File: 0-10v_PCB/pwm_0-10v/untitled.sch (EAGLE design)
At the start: 3 parts, among them U1 OP07CDR

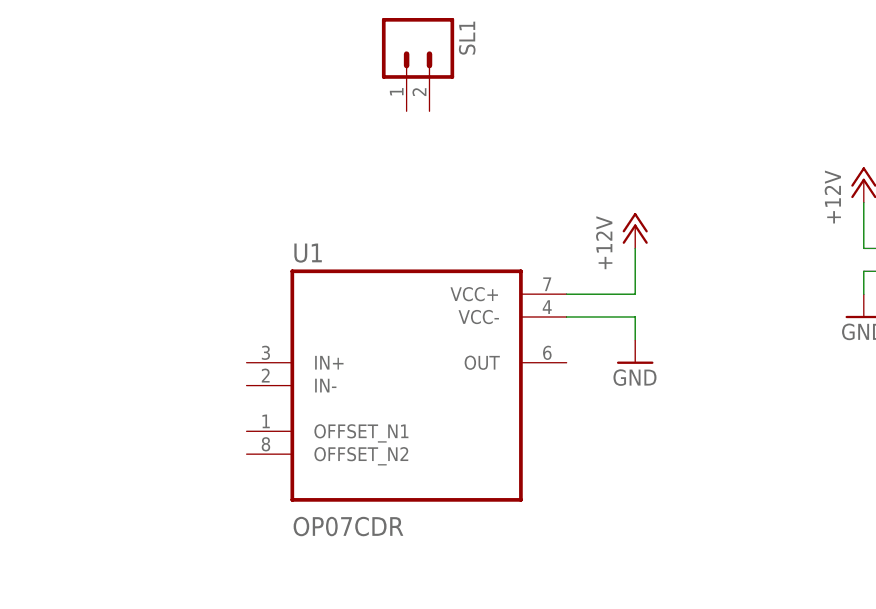
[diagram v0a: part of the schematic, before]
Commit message: added analog circuitry
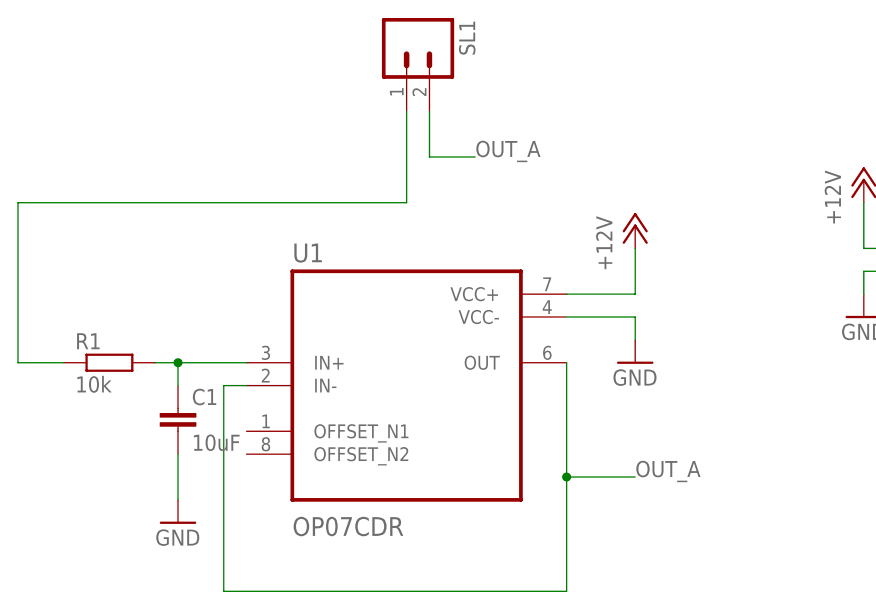
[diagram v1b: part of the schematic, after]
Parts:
- added C1: 10uF, rcl:C-EUC0805
- added R1: 10k, rcl:R-EU_M0805
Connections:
- new net N$1: R1.1, SL1.1
- new net N$2: C1.1, R1.2, U1.IN+
- new net N$3: SL1.2
- new net OUT_A: U1.IN-, U1.OUT
- net GND: now also C1.2
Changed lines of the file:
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@@
 <part name="P+2" library="supply1" library_urn="urn:adsk.eagle:library:371" deviceset="+12V" device=""/>
 <part name="GND2" library="supply1" library_urn="urn:adsk.eagle:library:371" deviceset="GND" device=""/>
+<part name="R1" library="rcl" library_urn="urn:adsk.eagle:library:334" deviceset="R-EU_" device="M0805" package3d_urn="urn:adsk.eagle:package:23556/2" value="10k"/>
+<part name="C1" library="rcl" library_urn="urn:adsk.eagle:library:334" deviceset="C-EU" device="C0805" package3d_urn="urn:adsk.eagle:package:23617/2" value="10uF"/>
+<part name="GND3" library="supply1" library_urn="urn:adsk.eagle:library:371" deviceset="GND" device=""/>
 </parts>
 <sheets>
@@
 <attribute name="VALUE" x="83.82" y="71.12" size="1.778" layer="96"/>
 </instance>
+<instance part="R1" gate="G$1" x="27.94" y="73.66" smashed="yes">
+<attribute name="NAME" x="24.13" y="75.1586" size="1.778" layer="95"/>
+<attribute name="VALUE" x="24.13" y="70.358" size="1.778" layer="96"/>
+</instance>
+<instance part="C1" gate="G$1" x="35.56" y="68.58" smashed="yes">
+<attribute name="NAME" x="37.084" y="68.961" size="1.778" layer="95"/>
+<attribute name="VALUE" x="37.084" y="63.881" size="1.778" layer="96"/>
+</instance>
+<instance part="GND3" gate="1" x="35.56" y="55.88" smashed="yes">
+<attribute name="VALUE" x="33.02" y="53.34" size="1.778" layer="96"/>
+</instance>
 </instances>
 <busses>
@@
 <wire x1="86.36" y1="78.74" x2="86.36" y2="76.2" width="0.1524" layer="91"/>
 </segment>
+<segment>
+<pinref part="C1" gate="G$1" pin="2"/>
+<pinref part="GND3" gate="1" pin="GND"/>
+<wire x1="35.56" y1="63.5" x2="35.56" y2="58.42" width="0.1524" layer="91"/>
+</segment>
 </net>
 <net name="+12V" class="0">
@@
 <pinref part="P+2" gate="1" pin="+12V"/>
 <wire x1="86.36" y1="81.28" x2="86.36" y2="86.36" width="0.1524" layer="91"/>
+</segment>
+</net>
+<net name="N$1" class="0">
+<segment>
+<pinref part="SL1" gate="G$1" pin="1"/>
+<wire x1="60.96" y1="101.6" x2="60.96" y2="91.44" width="0.1524" layer="91"/>
+<wire x1="60.96" y1="91.44" x2="17.78" y2="91.44" width="0.1524" layer="91"/>
+<wire x1="17.78" y1="91.44" x2="17.78" y2="73.66" width="0.1524" layer="91"/>
+<pinref part="R1" gate="G$1" pin="1"/>
+<wire x1="17.78" y1="73.66" x2="22.86" y2="73.66" width="0.1524" layer="91"/>
+</segment>
+</net>
+<net name="N$2" class="0">
+<segment>
+<pinref part="R1" gate="G$1" pin="2"/>
+<pinref part="U1" gate="A" pin="IN+"/>
+<wire x1="33.02" y1="73.66" x2="35.56" y2="73.66" width="0.1524" layer="91"/>
+<pinref part="C1" gate="G$1" pin="1"/>
+<wire x1="35.56" y1="73.66" x2="43.18" y2="73.66" width="0.1524" layer="91"/>
+<wire x1="35.56" y1="71.12" x2="35.56" y2="73.66" width="0.1524" layer="91"/>
+<junction x="35.56" y="73.66"/>
+</segment>
+</net>
+<net name="OUT_A" class="0">
+<segment>
+<pinref part="U1" gate="A" pin="IN-"/>
+<wire x1="43.18" y1="71.12" x2="40.64" y2="71.12" width="0.1524" layer="91"/>
+<wire x1="40.64" y1="71.12" x2="40.64" y2="48.26" width="0.1524" layer="91"/>
+<wire x1="40.64" y1="48.26" x2="78.74" y2="48.26" width="0.1524" layer="91"/>
+<pinref part="U1" gate="A" pin="OUT"/>
+<wire x1="78.74" y1="48.26" x2="78.74" y2="60.96" width="0.1524" layer="91"/>
+<wire x1="78.74" y1="60.96" x2="78.74" y2="73.66" width="0.1524" layer="91"/>
+<wire x1="78.74" y1="60.96" x2="86.36" y2="60.96" width="0.1524" layer="91"/>
+<junction x="78.74" y="60.96"/>
+<label x="86.36" y="60.96" size="1.778" layer="95"/>
+<label x="68.58" y="96.52" size="1.778" layer="95"/>
+</segment>
+</net>
+<net name="N$3" class="0">
+<segment>
+<pinref part="SL1" gate="G$1" pin="2"/>
+<wire x1="63.5" y1="101.6" x2="63.5" y2="96.52" width="0.1524" layer="91"/>
+<wire x1="63.5" y1="96.52" x2="68.58" y2="96.52" width="0.1524" layer="91"/>
 </segment>
 </net>
@@
 packages will not be understood (or retained) with this version.
 </note>
+<note version="8.4" severity="warning">
+Since Version 8.4, EAGLE supports properties for SPICE simulation.
+Probes in schematics and SPICE mapping objects found in parts and library devices
+will not be understood with this version. Update EAGLE to the latest version
+for full support of SPICE simulation.
+</note>
 </compatibility>

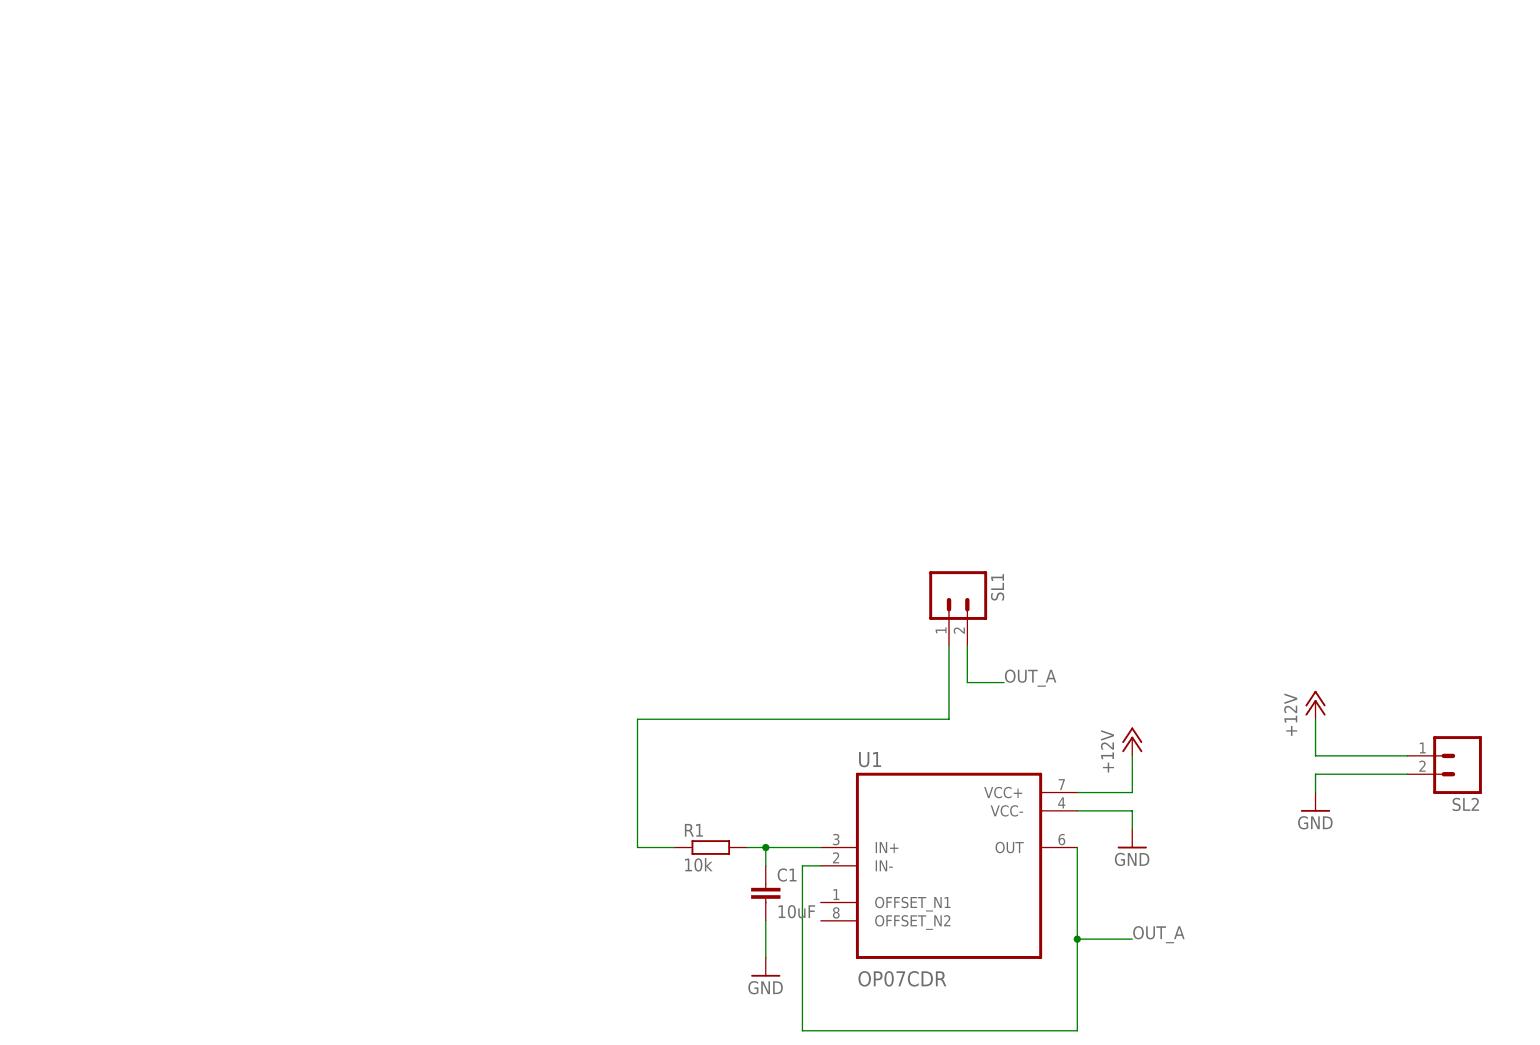
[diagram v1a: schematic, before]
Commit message: part placement completed
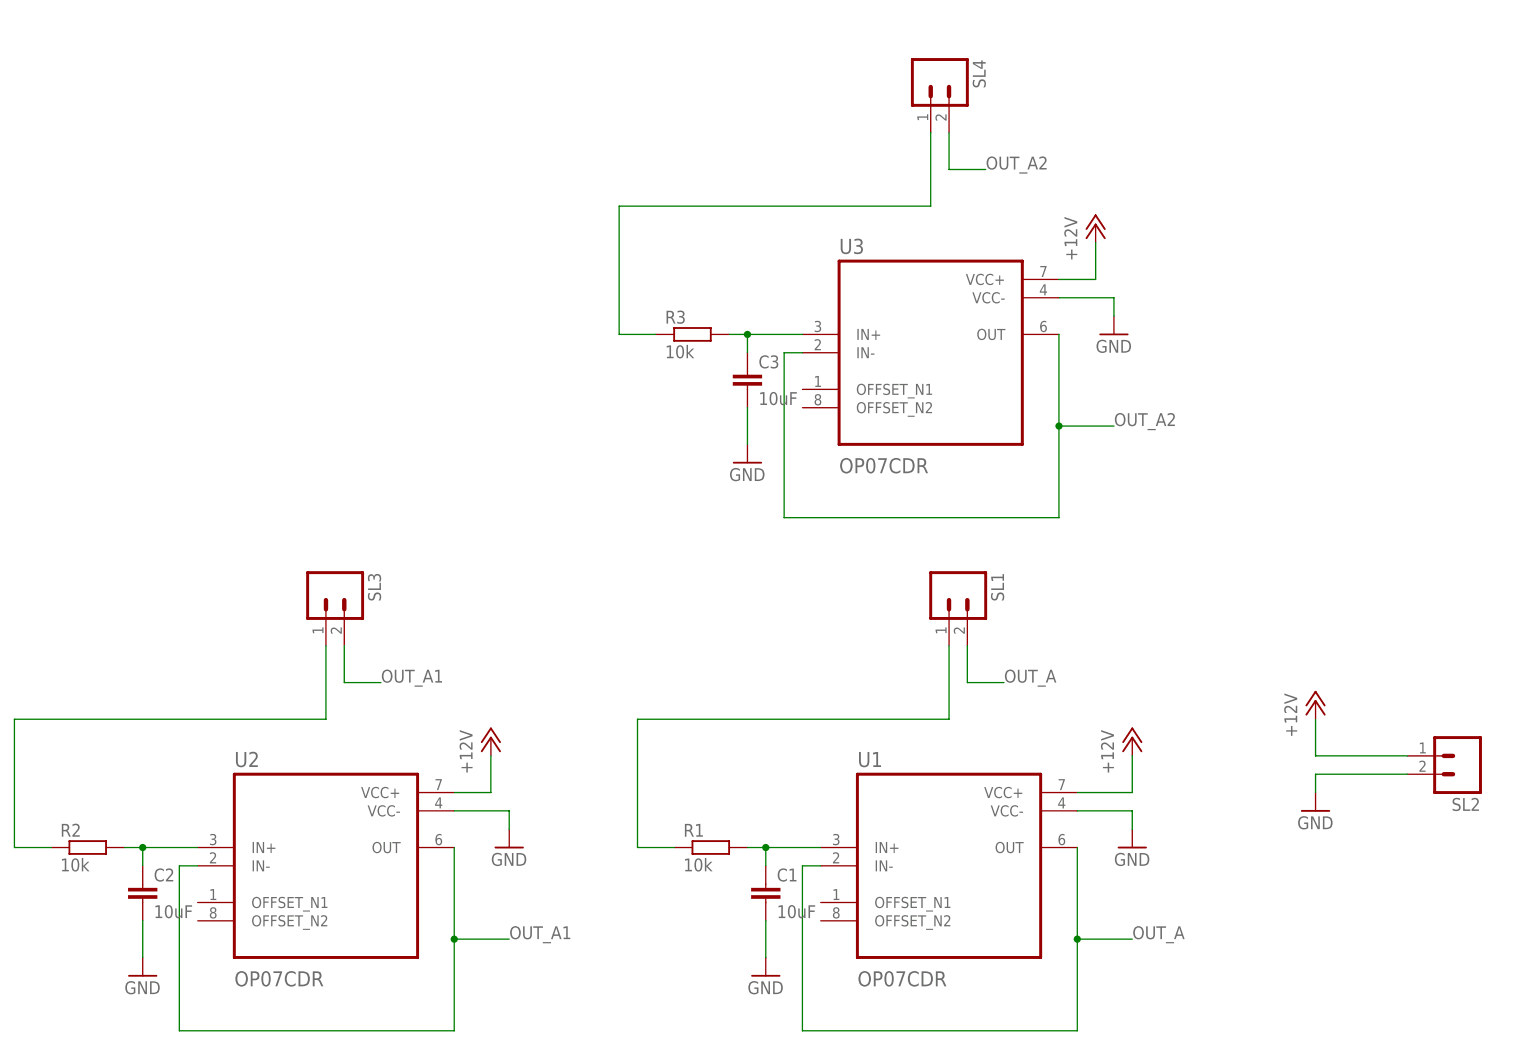
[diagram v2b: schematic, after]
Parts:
- added C2, C3: 10uF, rcl:C-EUC0805
- added R2, R3: 10k, rcl:R-EU_M0805
- added SL3, SL4: (no value), con-amp-quick:M02
- added U2, U3: OP07CDR, OP07CDR:OP07CDR
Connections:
- new net N$4: C2.1, R2.2, U2.IN+
- new net N$5: R3.1, SL4.1
- new net N$6: C3.1, R3.2, U3.IN+
- new net OUT_A1: SL3.2, U2.IN-, U2.OUT
- new net OUT_A2: SL4.2, U3.IN-, U3.OUT
- net +12V: now also U2.VCC+, U3.VCC+
- net GND: now also C2.2, C3.2, U2.VCC-, U3.VCC-
- net N$3: now also R2.1, SL3.1; no longer SL1.2
- net OUT_A: now also SL1.2

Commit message: changed screw terminals to correct size
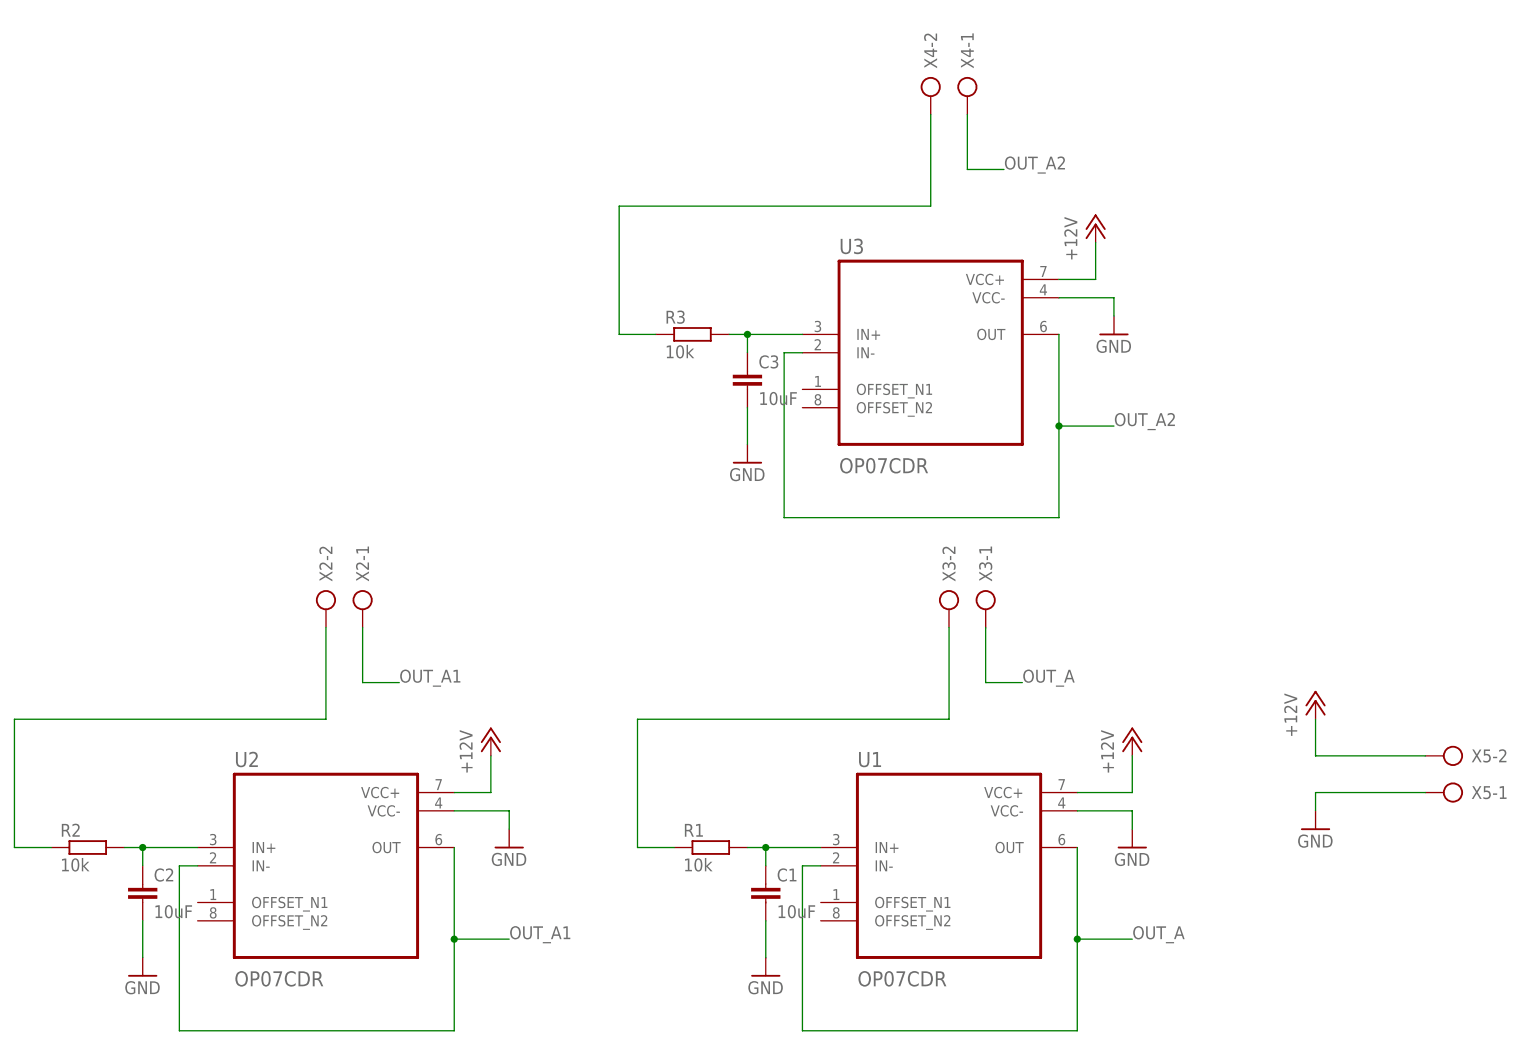
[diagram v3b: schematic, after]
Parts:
- removed SL1, SL2, SL3, SL4: (no value), con-amp-quick:M02
- added X2, X3, X4, X5: (no value), con-ptr500:AK500/2
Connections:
- net +12V: now also X5-2.KL; no longer SL2.1
- net GND: now also X5-1.KL; no longer SL2.2
- net N$1: now also X3-2.KL; no longer SL1.1
- net N$3: now also X2-2.KL; no longer SL3.1
- net N$5: now also X4-2.KL; no longer SL4.1
- net OUT_A: now also X3-1.KL; no longer SL1.2
- net OUT_A1: now also X2-1.KL; no longer SL3.2
- net OUT_A2: now also X4-1.KL; no longer SL4.2
